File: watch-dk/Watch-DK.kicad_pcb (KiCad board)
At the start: 4 copper layers, 100 x 70 mm, 126 parts, among them IC401 nPM1300-QEXX, IC501 APDS-9306-065, IC502 BMI270, IC503 LIS2MDLTR, IC504 BMP581, IC505 DRV2603RUNT, IC506 PCA9306JK, IC507 RV-8263-C8, IC601 FAN5622SX, IC602 USBLC6-2P6, IC603 MX25U51245GZ4I00, IC604 NTS0104GU12, M601 NORA-B106, Q401 PMZ550UNEYL, Q402 PMZ550UNEYL, Q403 PMZ550UNEYL, Q404 PMZB320UPEYL, Q501 PMZB320UPEYL, X401 Battery, X402 Battery, X403 Power, X501 Current, X502 I2S, X503 Current, X504 I2C, X505 Current, X506 Current, X507 Current, X508 Current, X509 Motor, X510 Current, X601 DEBUG, X602 Current, X603 Device, X604 UART, X605 GPIO, X606 Current, X607 IO Current, X608 Display, X609 Touch Current, X610 LED Current

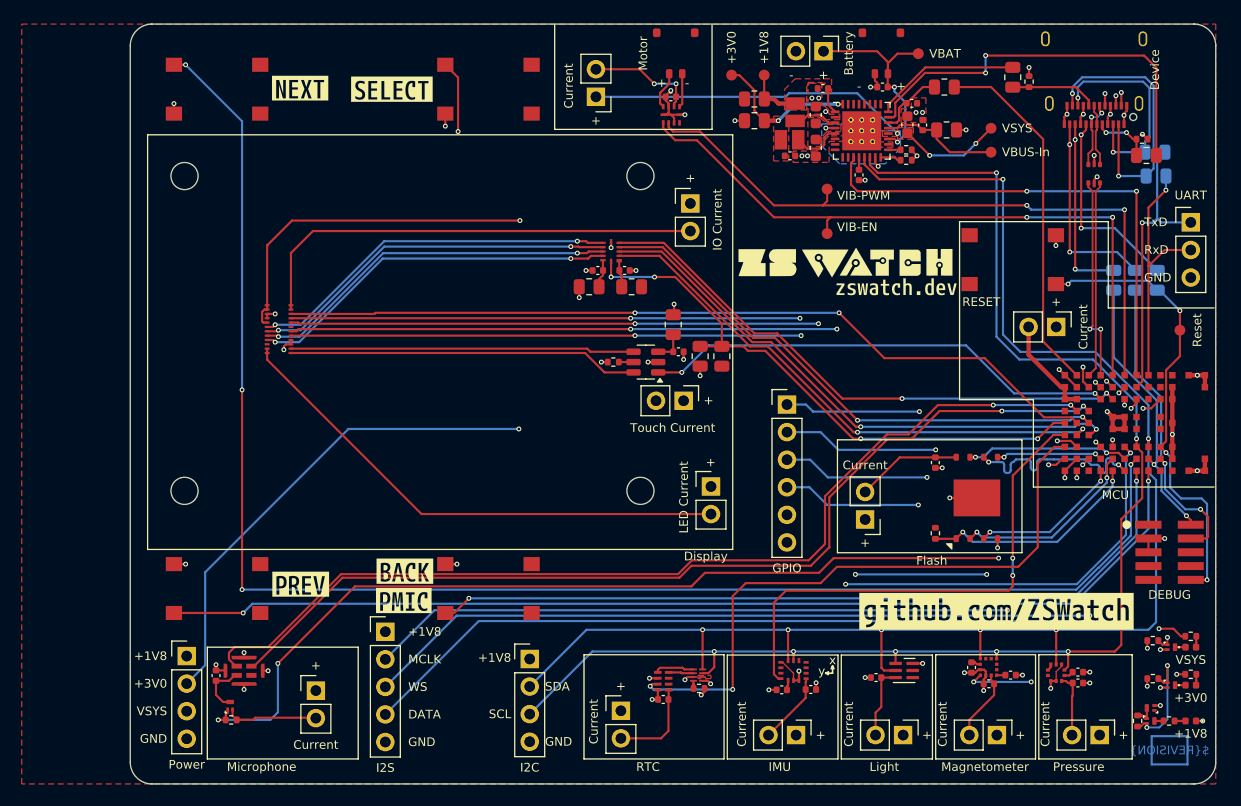
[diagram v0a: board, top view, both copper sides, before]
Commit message: Feature: Issue #145
- Update symbols

Signed-off-by: Daniel Kampert <DanielKampert@kampis-elektroecke.de>
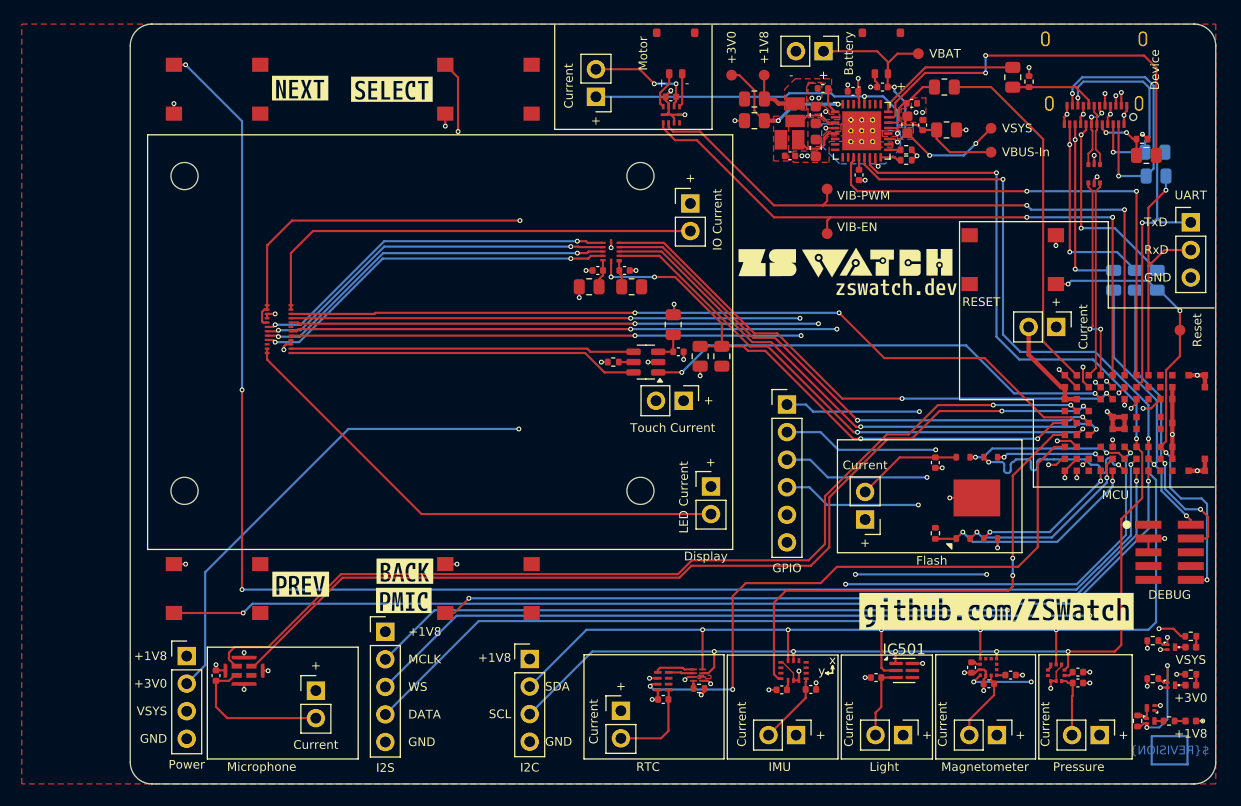
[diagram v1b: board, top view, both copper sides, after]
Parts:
- removed Q501: PMZB320UPEYL, Package_DFN_Kampi:DFN-1006-3
- removed R501: 100k, Resistor_SMD:R_0402_1005Metric
- added C410: 10u, Capacitor_SMD:C_0402_1005Metric, F.Cu at (224.6, 120.2)
- IC501: footprint Broadcom:Broadcom_DFN-6_2x2mm_P0.65mm -> OptoDevice:Broadcom_DFN-6_2x2mm_P0.65mm
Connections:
- IC401 pad 28: unconnected-(IC401-LSIN1/VINLDO1-Pad28) -> /Project Architecture/Peripherals/VSYS
- IC401 pad 29: unconnected-(IC401-LSOUT1/VOUTLDO1-Pad29) -> /Project Architecture/Peripherals/VMIC
- M601 pad D3: /Project Architecture/MCU/MIC-EN -> unconnected-(M601B-P0.07/AIN3-PadD3)
- X503 pad 1: +1V8 -> /Project Architecture/Peripherals/VMIC
- X503 pad 2: Net-(X503-Pin_2) -> Net-(MK501-VDD)
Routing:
- net /Project Architecture/Peripherals/VMIC: track 0.00 -> 103.0 mm, vias 0 -> 1
- net /Project Architecture/MCU/MIC-EN: track 97.8 -> 0.00 mm, vias 4 -> 0
- net Net-(MK501-VDD): track 4.99 -> 14.2 mm
- net Net-(X503-Pin_2): track 8.50 -> 0.00 mm
- net /Project Architecture/Peripherals/VSYS: track 198.2 -> 200.2 mm, vias 5 -> 6
- net GND: track 81.2 -> 81.8 mm, vias 65 -> 66
- net /Project Architecture/MCU/MCLK: track 83.6 -> 83.1 mm

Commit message: Silkscreen tweaking and formatting.
- Remove ZSWatch logo and url as it is part of UV print
- Add silkscreen to HR header
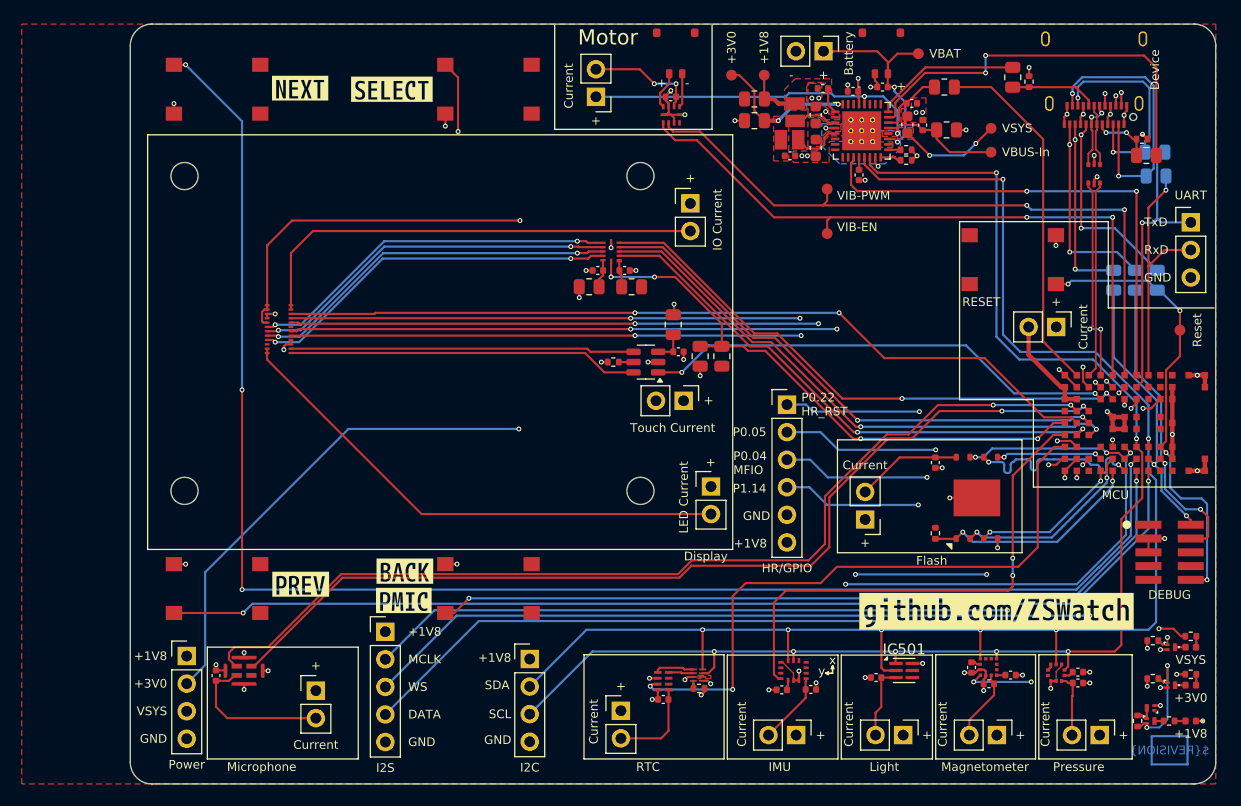
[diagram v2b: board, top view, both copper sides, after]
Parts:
- removed G***: LOGO, footprints:Logo
- removed kibuzzard-68304463: G***, kibuzzard-68304463
- X605: value GPIO -> HR/GPIO
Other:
- board text added: "P0.04 MFIO"
- board text added: "P0.05"
- board text added: "P0.22 HR_RST"
- board text added: "P1.14"

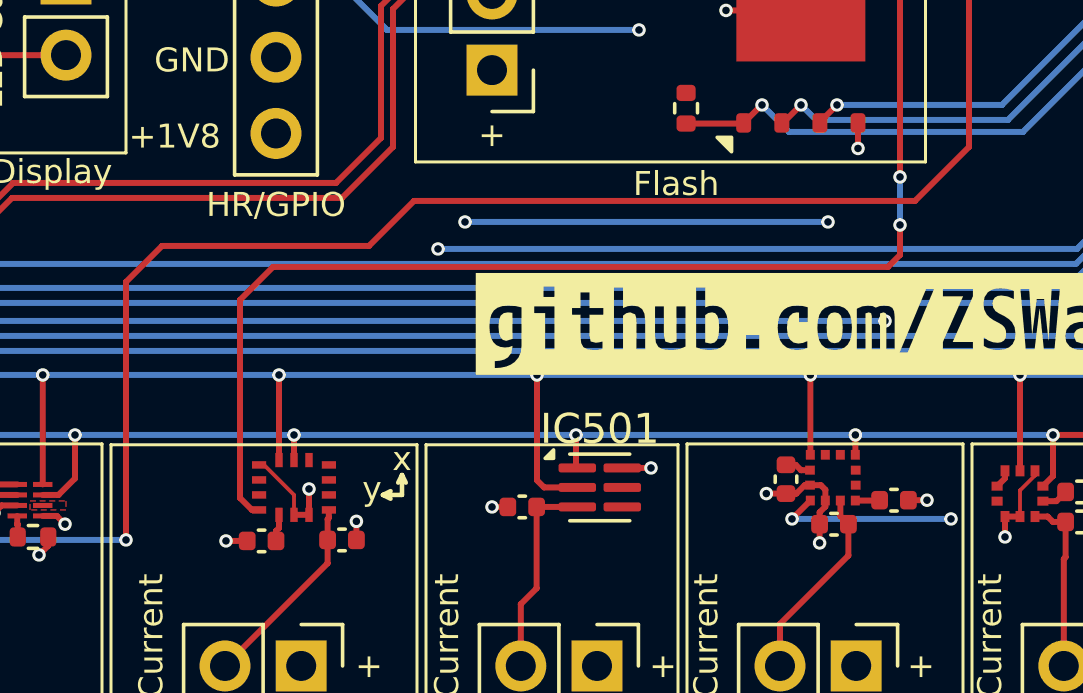
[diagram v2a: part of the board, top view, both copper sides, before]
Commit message: Bug: Issue #146
Signed-off-by: Daniel Kampert <DanielKampert@kampis-elektroecke.de>
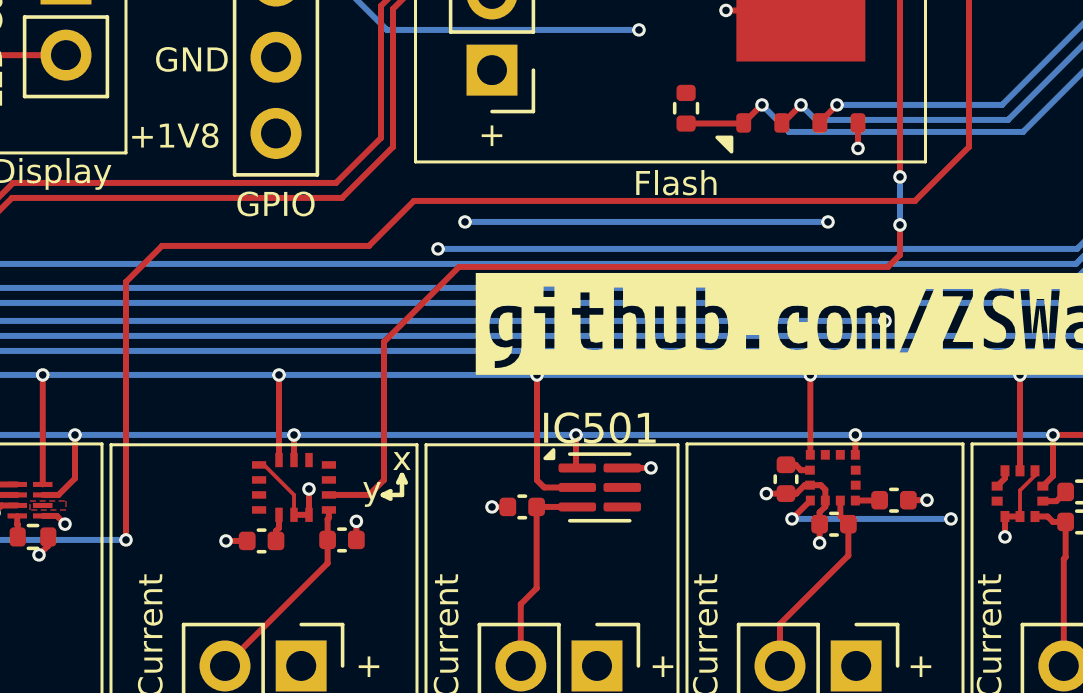
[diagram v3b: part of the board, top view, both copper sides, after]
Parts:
- X605: value HR/GPIO -> GPIO
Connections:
- IC502 pad 4: /Project Architecture/MCU/BMI270-INT -> unconnected-(IC502-INT1-Pad4)
- IC502 pad 9: unconnected-(IC502-INT2-Pad9) -> /Project Architecture/MCU/BMI270-INT
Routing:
- net /Project Architecture/MCU/BMI270-INT: track 46.6 -> 41.6 mm

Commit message: Feature: Issue #149
Signed-off-by: Daniel Kampert <DanielKampert@kampis-elektroecke.de>
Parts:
- added TP503: MIC-CLK, TestPoint:TestPoint_Pad_D1.0mm, F.Cu at (172.2, 172.9)
- added TP504: MIC-Data, TestPoint:TestPoint_Pad_D1.0mm, F.Cu at (170.2, 176.6)
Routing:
- net /Project Architecture/MCU/MIC-DATA: track 92.0 -> 99.9 mm, vias 2 -> 4
- net /Project Architecture/MCU/MIC-CLK: track 90.0 -> 92.1 mm
